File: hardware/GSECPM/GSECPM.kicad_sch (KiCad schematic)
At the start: 43 parts, among them J1 N2-Bottle PT, J10 Ignition E-Match, J11 QD E-Match, J12 Radio Module Connector, J13 Purge Servo, J14 Power Input, J15 Internal Cooling, J16 Nitrous Cooling, J17 Load Cell + Amp, J2 K-Bottle TC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

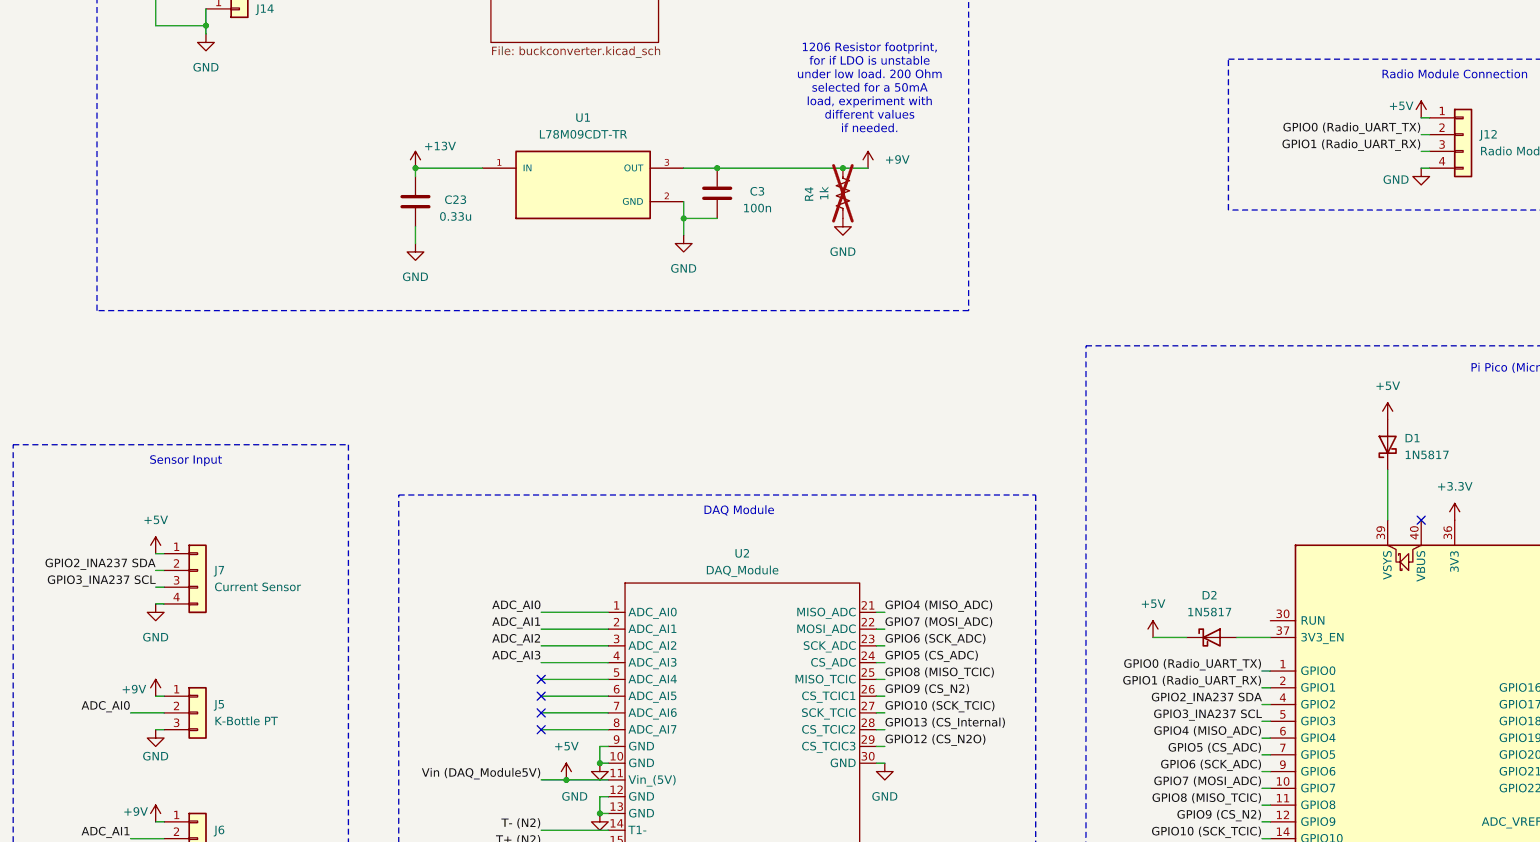
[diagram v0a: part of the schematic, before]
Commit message: Swapped positions of radio and INA237 conns for optimized current loop. Swapped 9V LDO to a TI model that supports newer ceramic caps better than the original STM legacy LDO
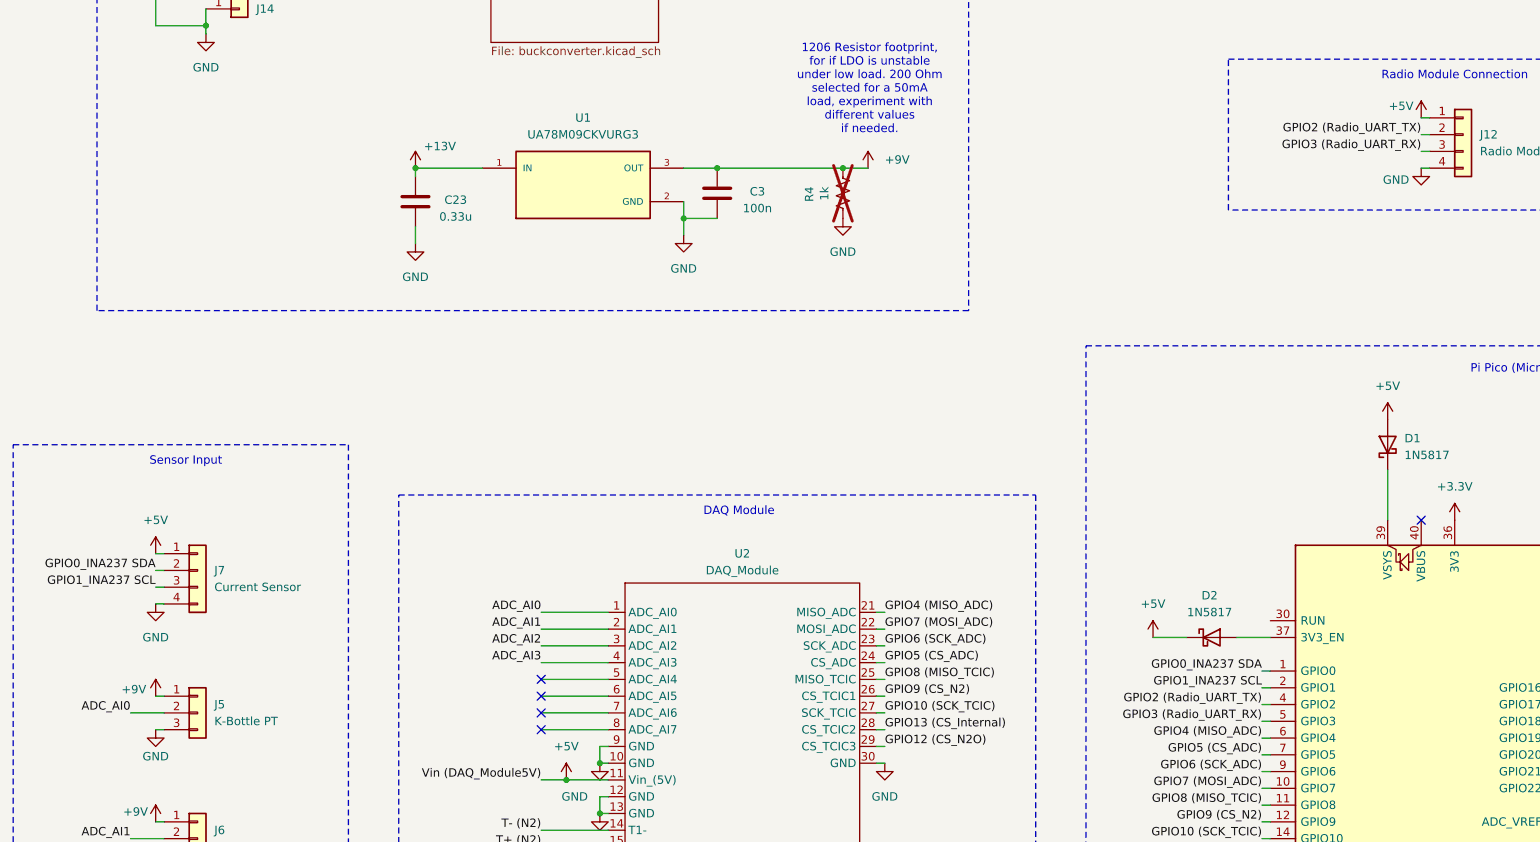
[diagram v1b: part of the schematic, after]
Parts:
- U1: value L78M09CDT-TR -> UA78M09CKVURG3; DigiKey https://www.digikey.com/en/products/detail/stmicroelectroni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 -> https://www.digikey.com/en/products/detail/texas-instrument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
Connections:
- net GPIO0 (Radio_UART_TX) renamed GPIO0_INA237 SDA
- net GPIO0_INA237 SDA: now also J7.2 (Pin_2); no longer J12.2 (Pin_2)
- net GPIO1 (Radio_UART_RX) renamed GPIO1_INA237 SCL
- net GPIO1_INA237 SCL: now also J7.3 (Pin_3); no longer J12.3 (Pin_3)
- net GPIO2_INA237 SDA renamed GPIO2 (Radio_UART_TX)
- net GPIO2 (Radio_UART_TX): now also J12.2 (Pin_2); no longer J7.2 (Pin_2)
- net GPIO3_INA237 SCL renamed GPIO3 (Radio_UART_RX)
- net GPIO3 (Radio_UART_RX): now also J12.3 (Pin_3); no longer J7.3 (Pin_3)
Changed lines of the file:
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@@
 		)
 	)
-	(label "GPIO0 (Radio_UART_TX)"
-		(at 205.74 147.32 180)
-		(effects
-			(font
-				(size 1.27 1.27)
-			)
-			(justify right bottom)
-		)
-	)
 	(label "ADC_AI2"
 		(at 96.52 143.51 180)
@@
 		)
 	)
-	(label "GPIO0 (Radio_UART_TX)"
+	(label "GPIO2 (Radio_UART_TX)"
 		(at 229.87 66.04 180)
 		(effects
@@
 		)
 	)
-	(label "GPIO3_INA237 SCL"
+	(label "GPIO1_INA237 SCL"
 		(at 38.1 134.62 180)
 		(effects
@@
 		)
 	)
-	(label "GPIO1 (Radio_UART_RX)"
-		(at 205.74 149.86 180)
-		(effects
-			(font
-				(size 1.27 1.27)
-			)
-			(justify right bottom)
-		)
-	)
 	(label "ADC_AI1"
 		(at 34.29 172.72 180)
@@
 		)
 	)
-	(label "GPIO3_INA237 SCL"
-		(at 205.74 154.94 180)
+	(label "GPIO2 (Radio_UART_TX)"
+		(at 205.74 152.4 180)
 		(effects
 			(font
@@
 		)
 	)
-	(label "GPIO2_INA237 SDA"
-		(at 205.74 152.4 180)
+	(label "GPIO5 (CS_ADC)"
+		(at 148.59 146.05 0)
+		(effects
+			(font
+				(size 1.27 1.27)
+			)
+			(justify left bottom)
+		)
+	)
+	(label "T- (Internal)"
+		(at 96.52 176.53 180)
 		(effects
 			(font
@@
 		)
 	)
-	(label "GPIO5 (CS_ADC)"
-		(at 148.59 146.05 0)
+	(label "GPIO3 (Radio_UART_RX)"
+		(at 205.74 154.94 180)
 		(effects
 			(font
 				(size 1.27 1.27)
 			)
-			(justify left bottom)
+			(justify right bottom)
 		)
 	)
-	(label "T- (Internal)"
-		(at 96.52 176.53 180)
+	(label "GPIO1_INA237 SCL"
+		(at 205.74 149.86 180)
 		(effects
 			(font
@@
 		)
 	)
+	(label "GPIO0_INA237 SDA"
+		(at 205.74 147.32 180)
+		(effects
+			(font
+				(size 1.27 1.27)
+			)
+			(justify right bottom)
+		)
+	)
 	(label "Vin (DAQ_Module5V)"
 		(at 96.52 163.83 180)
@@
 		)
 	)
-	(label "GPIO2_INA237 SDA"
+	(label "GPIO0_INA237 SDA"
 		(at 38.1 132.08 180)
 		(effects
@@
 		)
 	)
-	(label "GPIO1 (Radio_UART_RX)"
+	(label "GPIO3 (Radio_UART_RX)"
 		(at 229.87 68.58 180)
 		(effects
@@
 			)
 		)
-		(property "Value" "L78M09CDT-TR"
+		(property "Value" "UA78M09CKVURG3"
 			(at 102.87 66.04 0)
 			(effects
@@
 			)
 		)
-		(property "Datasheet" "https://www.st.com/content/ccc/resource/technical/document/datasheet/d7/5f/dc/5c/d5/b6/48/7c/CD00000447.pdf/files/CD00000447.pdf/jcr:content/translations/en.CD00000447.pdf"
+		(property "Datasheet" "https://www.ti.com/lit/ds/slvs059v/slvs059v.pdf?ts=1763139695419&ref_url=https%253A%252F%252Fszlcscdz.cn%252F"
 			(at 102.87 73.66 0)
 			(effects
@@
 			)
 		)
-		(property "DigiKey" "https://www.digikey.com/en/products/detail/stmicroelectronics/L78M09CDT-TR/585732"
+		(property "DigiKey" "https://www.digikey.com/en/products/detail/texas-instruments/UA78M09CKVURG3/1000275"
 			(at 102.87 73.66 0)
 			(effects
@@
 		)
 		(instances
-			(project "GSED_0001"
+			(project "GSECPM"
 				(path "/264b8d8f-c165-4609-b867-e24f99960723"
 					(page "5")

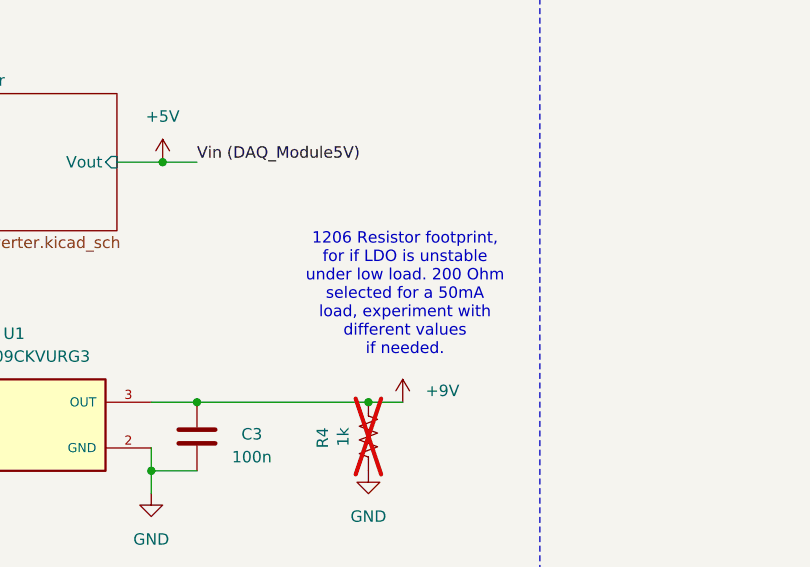
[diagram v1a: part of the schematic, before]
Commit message: Better buck converter positioning with inductor further from analog signals. Improved via stitching and fixed split ground planes somewhat except for Manhattans
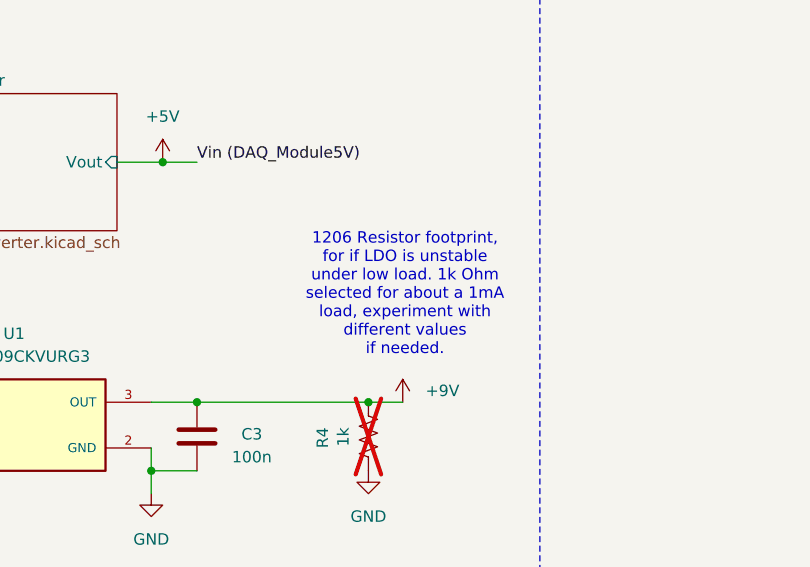
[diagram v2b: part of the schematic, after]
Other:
- note added: "1206 Resistor footprint, for if LDO is unstable under low load. 1k Ohm selected for about a 1mA load, experiment with different values if needed."
- note removed: "1206 Resistor footprint, for if LDO is unstable under low load. 200 Ohm selected for a 50mA load, experiment with different values if needed."
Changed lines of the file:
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@@
 		)
 	)
-	(text "1206 Resistor footprint,\nfor if LDO is unstable\nunder low load. 200 Ohm\nselected for a 50mA\nload, experiment with\ndifferent values \nif needed."
+	(text "1206 Resistor footprint,\nfor if LDO is unstable\nunder low load. 1k Ohm\nselected for about a 1mA\nload, experiment with\ndifferent values \nif needed."
 		(exclude_from_sim no)
 		(at 146.304 59.182 0)

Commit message: Finished PCBs with production files
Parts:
- removed C23: 0.33u, Capacitor_SMD:C_1206_3216Metric, symbol Device:C
- added C4: 10u, Capacitor_SMD:C_1210_3225Metric, symbol Device:C
- C3: value 100n -> 10u; footprint Capacitor_SMD:C_0603_1608Metric -> Capacitor_SMD:C_1210_3225Metric; DigiKey https://www.digikey.com/en/products/detail/samsung-electro-mechanics/CL10B104KB8NNNC/3886658 -> https://www.digikey.com/en/products/detail/samsung-electro-mechanics/CL32B106KBJNNNE/3889045
- Q1: value BUK6Y33-60PX -> PSMP033-60YEX; DigiKey https://www.digikey.com/en/products/detail/nexperia-usa-inc/BUK6Y33-60PX/12325065 -> https://www.digikey.com/en/products/detail/nexperia-usa-inc/PSMP033-60YEX/18689473
- Q3, U4, U5: DigiKey https://www.digikey.com/en/products/detail/nexperia-usa-inc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 -> https://www.digikey.com/en/products/detail/diodes-incorpora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
- U1: value UA78M09CKVURG3 -> BD90C0AFP-CE2; MANUFACTURER STMicroelectronics -> Rohm Semiconductor
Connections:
- net +13V: now also C4.2
- net GND: now also C4.1
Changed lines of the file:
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@@
 			)
 		)
-		(property "Value" "BUK6Y33-60PX"
+		(property "Value" "PSMP033-60YEX"
 			(at 381 239.522 90)
 			(effects
@@
 			)
 		)
-		(property "Datasheet" "https://assets.nexperia.com/documents/data-sheet/BUK6Y33-60P.pdf"
+		(property "Datasheet" "PSMP033-60YEX"
 			(at 372.11 223.52 0)
 			(effects
@@
 			)
 		)
-		(property "DigiKey" "https://www.digikey.com/en/products/detail/nexperia-usa-inc/BUK6Y33-60PX/12325065"
+		(property "DigiKey" "https://www.digikey.com/en/products/detail/nexperia-usa-inc/PSMP033-60YEX/18689473"
 			(at 372.11 223.52 0)
 			(effects
@@
 		)
 		(property "Value" "+V_Servo"
-			(at 380.746 233.426 0)
+			(at 389.128 231.902 0)
 			(effects
 				(font
@@
 	)
 	(symbol
+		(lib_id "Device:C")
+		(at 77.47 76.2 180)
+		(unit 1)
+		(exclude_from_sim no)
+		(in_bom yes)
+		(on_board yes)
+		(dnp no)
+		(property "Reference" "C4"
+			(at 83.566 75.946 0)
+			(effects
+				(font
+					(size 1.27 1.27)
+				)
+			)
+		)
+		(property "Value" "10u"
+			(at 83.566 78.486 0)
+			(effects
+				(font
+					(size 1.27 1.27)
+				)
+			)
+		)
+		(property "Footprint" "Capacitor_SMD:C_1210_3225Metric"
+			(at 76.5048 72.39 0)
+			(effects
+				(font
+					(size 1.27 1.27)
+				)
+				(hide yes)
+			)
+		)
+		(property "Datasheet" "https://mm.digikey.com/Volume0/opasdata/d220001/medias/docus/41/CL32B106KBJNNNE_Spec.pdf"
+			(at 77.47 76.2 0)
+			(effects
+				(font
+					(size 1.27 1.27)
+				)
+				(hide yes)
+			)
+		)
+		(property "Description" ""
+			(at 77.47 76.2 0)
+			(effects
+				(font
+					(size 1.27 1.27)
+				)
+			)
+		)
+		(property "DigiKey" "https://www.digikey.com/en/products/detail/samsung-electro-mechanics/CL32B106KBJNNNE/3889045"
+			(at 77.47 76.2 0)
+			(effects
+				(font
+					(size 1.27 1.27)
+				)
+				(hide yes)
+			)
+		)
+		(pin "1"
+		)
+		(pin "2"
+		)
+		(instances
+			(project "GSECPM"
+				(path "/264b8d8f-c165-4609-b867-e24f99960723"
+					(reference "C4")
+					(unit 1)
+				)
+			)
+		)
+	)
+	(symbol
 		(lib_id "power:+5V")
 		(at 224.79 109.22 0)
@@
 	)
 	(symbol
-		(lib_id "Device:C")
-		(at 77.47 76.2 180)
-		(unit 1)
-		(exclude_from_sim no)
-		(in_bom yes)
-		(on_board yes)
-		(dnp no)
-		(property "Reference" "C23"
-			(at 83.566 75.946 0)
-			(effects
-				(font
-					(size 1.27 1.27)
-				)
-			)
-		)
-		(property "Value" "0.33u"
-			(at 83.566 78.486 0)
-			(effects
-				(font
-					(size 1.27 1.27)
-				)
-			)
-		)
-		(property "Footprint" "Capacitor_SMD:C_1206_3216Metric"
-			(at 76.5048 72.39 0)
-			(effects
-				(font
-					(size 1.27 1.27)
-				)
-				(hide yes)
-			)
-		)
-		(property "Datasheet" "https://www.samsungsem.com/resources/file/global/support/product_catalog/MLCC_Automotive.pdf"
-			(at 77.47 76.2 0)
-			(effects
-				(font
-					(size 1.27 1.27)
-				)
-				(hide yes)
-			)
-		)
-		(property "Description" ""
-			(at 77.47 76.2 0)
-			(effects
-				(font
-					(size 1.27 1.27)
-				)
-			)
-		)
-		(property "DigiKey" "https://www.digikey.com/en/products/detail/samsung-electro-mechanics/CL31B334KBH5PNF/7320560"
-			(at 77.47 76.2 0)
-			(effects
-				(font
-					(size 1.27 1.27)
-				)
-				(hide yes)
-			)
-		)
-		(pin "1"
-		)
-		(pin "2"
-		)
-		(instances
-			(project "GSED_0001"
-				(path "/264b8d8f-c165-4609-b867-e24f99960723"
-					(reference "C23")
-					(unit 1)
-				)
-			)
-		)
-	)
-	(symbol
 		(lib_id "power:+12V")
 		(at 146.05 71.12 0)
@@
 			)
 		)
-		(property "Datasheet" "~"
+		(property "Datasheet" "https://www.diodes.com/assets/Datasheets/BC846AW-BC848CW.pdf"
 			(at 393.446 217.932 0)
 			(effects
@@
 			)
 		)
-		(property "DigiKey" "https://www.digikey.com/en/products/detail/nexperia-usa-inc/BC847CW-135/1232291"
+		(property "DigiKey" "https://www.digikey.com/en/products/detail/diodes-incorporated/BC847CW-7-F/1099140"
 			(at 394.208 218.948 0)
 			(effects
@@
 			)
 		)
-		(property "Value" "100n"
+		(property "Value" "10u"
 			(at 129.286 77.216 0)
 			(effects
@@
 			)
 		)
-		(property "Footprint" "Capacitor_SMD:C_0603_1608Metric"
+		(property "Footprint" "Capacitor_SMD:C_1210_3225Metric"
 			(at 122.2248 71.12 0)
 			(effects
@@
 			)
 		)
-		(property "Datasheet" "https://mm.digikey.com/Volume0/opasdata/d220001/medias/docus/609/CL10B104KB8NNNC_Spec.pdf"
+		(property "Datasheet" "https://mm.digikey.com/Volume0/opasdata/d220001/medias/docus/41/CL32B106KBJNNNE_Spec.pdf"
 			(at 123.19 74.93 0)
 			(effects
@@
 			)
 		)
-		(property "DigiKey" "https://www.digikey.com/en/products/detail/samsung-electro-mechanics/CL10B104KB8NNNC/3886658"
+		(property "DigiKey" "https://www.digikey.com/en/products/detail/samsung-electro-mechanics/CL32B106KBJNNNE/3889045"
 			(at 123.19 74.93 0)
 			(effects
@@
 			)
 		)
-		(property "Datasheet" "https://assets.nexperia.com/documents/data-sheet/BAV199.pdf"
+		(property "Datasheet" "https://www.diodes.com/assets/Datasheets/ds30232.pdf"
 			(at 292.1 196.85 0)
 			(effects
@@
 			)
 		)
-		(property "DigiKey" "https://www.digikey.com/en/products/detail/nexperia-usa-inc/BAV199-215/763223?msockid=128e8e655193667d39a29db6508167d6"
+		(property "DigiKey" "https://www.digikey.com/en/products/detail/diodes-incorporated/BAV199-7-F/1033647"
 			(at 292.1 196.85 0)
 			(effects
@@
 			)
 		)
-		(property "Datasheet" "https://assets.nexperia.com/documents/data-sheet/BAV199.pdf"
+		(property "Datasheet" "https://www.diodes.com/assets/Datasheets/ds30232.pdf"
 			(at 287.02 161.29 0)
 			(effects
@@
 			)
 		)
-		(property "DigiKey" "https://www.digikey.com/en/products/detail/nexperia-usa-inc/BAV199-215/763223?msockid=128e8e655193667d39a29db6508167d6"
+		(property "DigiKey" "https://www.digikey.com/en/products/detail/diodes-incorporated/BAV199-7-F/1033647"
 			(at 287.02 161.29 0)
 			(effects
@@
 			)
 		)
-		(property "Value" "UA78M09CKVURG3"
+		(property "Value" "BD90C0AFP-CE2"
 			(at 102.87 66.04 0)
 			(effects
@@
 			)
 		)
-		(property "Datasheet" "https://www.ti.com/lit/ds/slvs059v/slvs059v.pdf?ts=1763139695419&ref_url=https%253A%252F%252Fszlcscdz.cn%252F"
+		(property "Datasheet" "https://www.ti.com/lit/ds/slvs059v/slvs059v.pdf?ts=1763737860687"
 			(at 102.87 73.66 0)
 			(effects
@@
 			)
 		)
-		(property "MANUFACTURER" "STMicroelectronics"
+		(property "MANUFACTURER" "Rohm Semiconductor"
 			(at 102.87 73.66 0)
 			(effects
